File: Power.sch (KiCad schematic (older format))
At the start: 0 parts

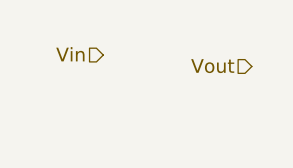
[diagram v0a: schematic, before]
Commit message: added SKY65366-21 schematic and footprint to library. Populated front end schematic with SKY and peripherial components. Added 3V6 output for power sub-schematic.
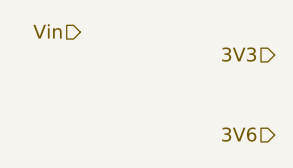
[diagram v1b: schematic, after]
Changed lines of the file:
@@
 Comment4 ""
 $EndDescr
-Text HLabel 3000 3300 0    60   Input ~ 0
+Text HLabel 2900 3200 0    60   Input ~ 0
 Vin
-Text HLabel 3650 3350 0    60   Input ~ 0
-Vout
+Text HLabel 3750 3300 0    60   Input ~ 0
+3V3
+Text HLabel 3750 3650 0    60   Input ~ 0
+3V6
 $EndSCHEMATC

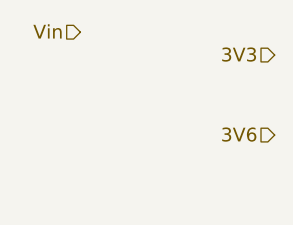
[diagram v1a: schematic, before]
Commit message: Fixed XOSC
-Changed 3V3 rail of XOSC to 1V8 as specified in datasheet
-Changed XOSC capacitor values to match the datasheet
-Added 1V8 rail to SFUSat-Radio.sch Transceiver and Power pages
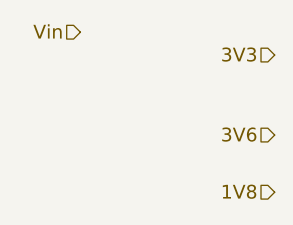
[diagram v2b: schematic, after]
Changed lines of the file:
@@
 Text HLabel 3750 3650 0    60   Input ~ 0
 3V6
+Text HLabel 3750 3900 0    60   Input ~ 0
+1V8
 $EndSCHEMATC

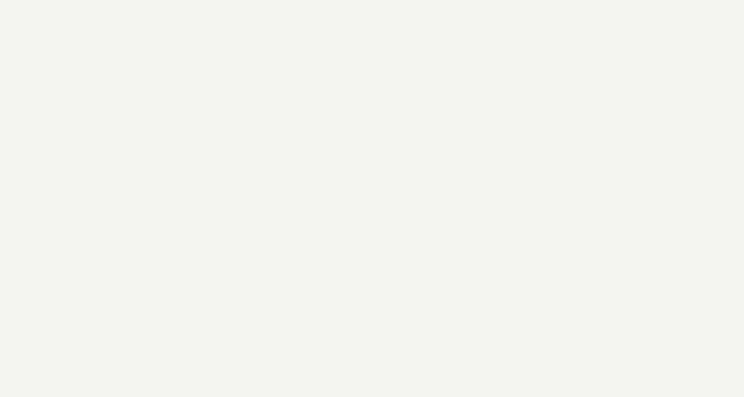
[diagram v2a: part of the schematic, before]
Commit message: Added schematic of RT9183HGM5 (TO263-5)
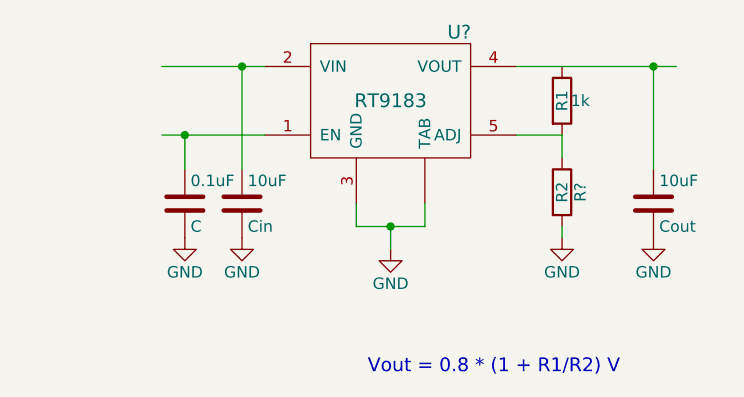
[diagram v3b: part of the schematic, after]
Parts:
- added 0.1uF: C, symbol C
- added 10uF: Cin, symbol C
- added 10uF: Cout, symbol C
- added 1k: R1, symbol R
- added R?: R2, symbol R
- added U?: RT9183, symbol RT9183
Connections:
- net labels added: GND
- wire segments 0 -> 13
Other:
- note added: "Vout = 0.8 * (1 + R1/R2) V\n"
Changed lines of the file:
@@
 Text HLabel 3750 3900 0    60   Input ~ 0
 1V8
+$Comp
+L RT9183 U?
+U 1 1 58770580
+P 5650 3000
+F 0 "U?" H 5950 3300 60  0000 C CNN
+F 1 "RT9183" H 5650 3000 60  0000 C CNN
+F 2 "" H 5650 3000 60  0001 C CNN
+F 3 "" H 5650 3000 60  0001 C CNN
+	1    5650 3000
+	1    0    0    -1
+$EndComp
+$Comp
+L C 10uF
+U 1 1 587706B0
+P 5000 3450
+F 0 "10uF" H 5025 3550 50  0000 L CNN
+F 1 "Cin" H 5025 3350 50  0000 L CNN
+F 2 "" H 5038 3300 50  0000 C CNN
+F 3 "" H 5000 3450 50  0000 C CNN
+	1    5000 3450
+	1    0    0    -1
+$EndComp
+$Comp
+L C 0.1uF
+U 1 1 58770789
+P 4750 3450
+F 0 "0.1uF" H 4775 3550 50  0000 L CNN
+F 1 "C" H 4775 3350 50  0000 L CNN
+F 2 "" H 4788 3300 50  0000 C CNN
+F 3 "" H 4750 3450 50  0000 C CNN
+	1    4750 3450
+	1    0    0    -1
+$EndComp
+$Comp
+L GND #PWR?
+U 1 1 58770941
+P 5650 3650
+F 0 "#PWR?" H 5650 3400 50  0001 C CNN
+F 1 "GND" H 5650 3500 50  0000 C CNN
+F 2 "" H 5650 3650 50  0000 C CNN
+F 3 "" H 5650 3650 50  0000 C CNN
+	1    5650 3650
+	1    0    0    -1
+$EndComp
+$Comp
+L C 10uF
+U 1 1 58770AC4
+P 6800 3450
+F 0 "10uF" H 6825 3550 50  0000 L CNN
+F 1 "Cout" H 6825 3350 50  0000 L CNN
+F 2 "" H 6838 3300 50  0000 C CNN
+F 3 "" H 6800 3450 50  0000 C CNN
+	1    6800 3450
+	1    0    0    -1
+$EndComp
+$Comp
+L GND #PWR?
+U 1 1 58770B93
+P 6800 3600
+F 0 "#PWR?" H 6800 3350 50  0001 C CNN
+F 1 "GND" H 6800 3450 50  0000 C CNN
+F 2 "" H 6800 3600 50  0000 C CNN
+F 3 "" H 6800 3600 50  0000 C CNN
+	1    6800 3600
+	1    0    0    -1
+$EndComp
+$Comp
+L GND #PWR?
+U 1 1 58770BD7
+P 6400 3600
+F 0 "#PWR?" H 6400 3350 50  0001 C CNN
+F 1 "GND" H 6400 3450 50  0000 C CNN
+F 2 "" H 6400 3600 50  0000 C CNN
+F 3 "" H 6400 3600 50  0000 C CNN
+	1    6400 3600
+	1    0    0    -1
+$EndComp
+$Comp
+L GND #PWR?
+U 1 1 58770CCB
+P 5000 3600
+F 0 "#PWR?" H 5000 3350 50  0001 C CNN
+F 1 "GND" H 5000 3450 50  0000 C CNN
+F 2 "" H 5000 3600 50  0000 C CNN
+F 3 "" H 5000 3600 50  0000 C CNN
+	1    5000 3600
+	1    0    0    -1
+$EndComp
+$Comp
+L GND #PWR?
+U 1 1 58770CE7
+P 4750 3600
+F 0 "#PWR?" H 4750 3350 50  0001 C CNN
+F 1 "GND" H 4750 3450 50  0000 C CNN
+F 2 "" H 4750 3600 50  0000 C CNN
+F 3 "" H 4750 3600 50  0000 C CNN
+	1    4750 3600
+	1    0    0    -1
+$EndComp
+Wire Wire Line
+	4650 2850 5100 2850
+Wire Wire Line
+	5000 2850 5000 3300
+Connection ~ 5000 2850
+Wire Wire Line
+	5100 3150 4650 3150
+Wire Wire Line
+	4750 3150 4750 3300
+Connection ~ 4750 3150
+Wire Wire Line
+	5500 3450 5500 3550
+Wire Wire Line
+	5800 3450 5800 3550
+Wire Wire Line
+	5800 3550 5500 3550
+Wire Wire Line
+	5650 3550 5650 3650
+Connection ~ 5650 3550
+Wire Wire Line
+	6200 2850 6900 2850
+Wire Wire Line
+	6800 2850 6800 3300
+Connection ~ 6800 2850
+Wire Wire Line
+	6200 3150 6400 3150
+Wire Wire Line
+	6400 3150 6400 3250
+Wire Wire Line
+	6400 3600 6400 3550
+$Comp
+L R R?
+U 1 1 58770EF4
+P 6400 3400
+F 0 "R?" V 6480 3400 50  0000 C CNN
+F 1 "R2" V 6400 3400 50  0000 C CNN
+F 2 "" V 6330 3400 50  0000 C CNN
+F 3 "" H 6400 3400 50  0000 C CNN
+	1    6400 3400
+	1    0    0    -1
+$EndComp
+$Comp
+L R 1k
+U 1 1 58770EC5
+P 6400 3000
+F 0 "1k" H 6480 3000 50  0000 C CNN
+F 1 "R1" V 6400 3000 50  0000 C CNN
+F 2 "" V 6330 3000 50  0000 C CNN
+F 3 "" H 6400 3000 50  0000 C CNN
+	1    6400 3000
+	1    0    0    -1
+$EndComp
+Text Notes 5550 4200 0    60   ~ 0
+Vout = 0.8 * (1 + R1/R2) V\n
 $EndSCHEMATC

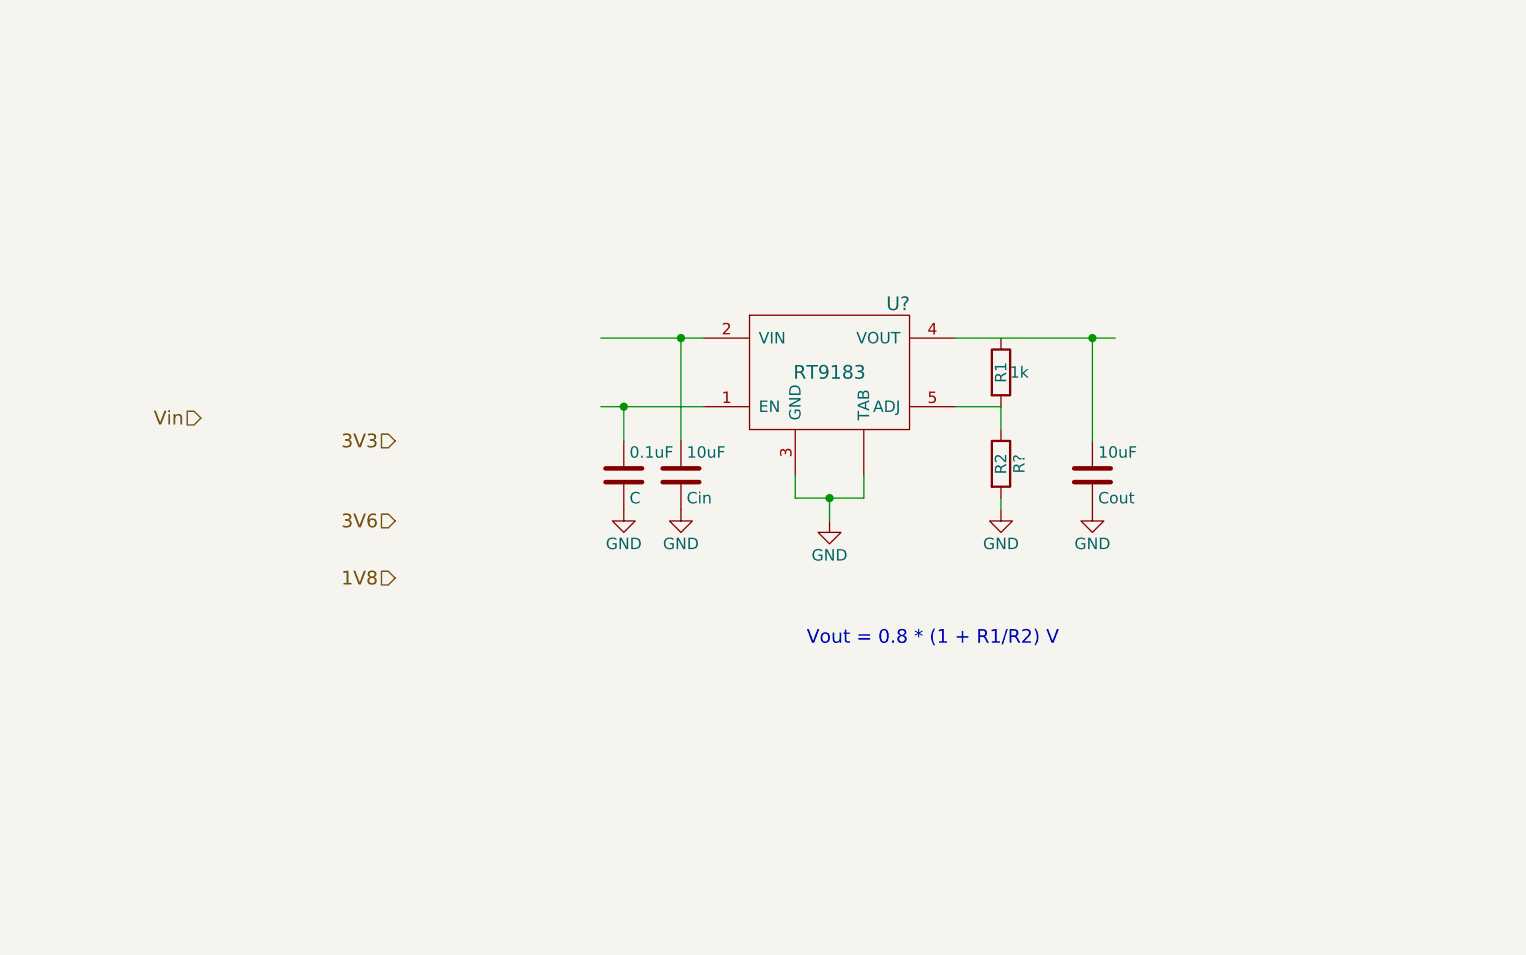
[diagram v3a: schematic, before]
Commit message: Added sch of TPS799 onto power sch
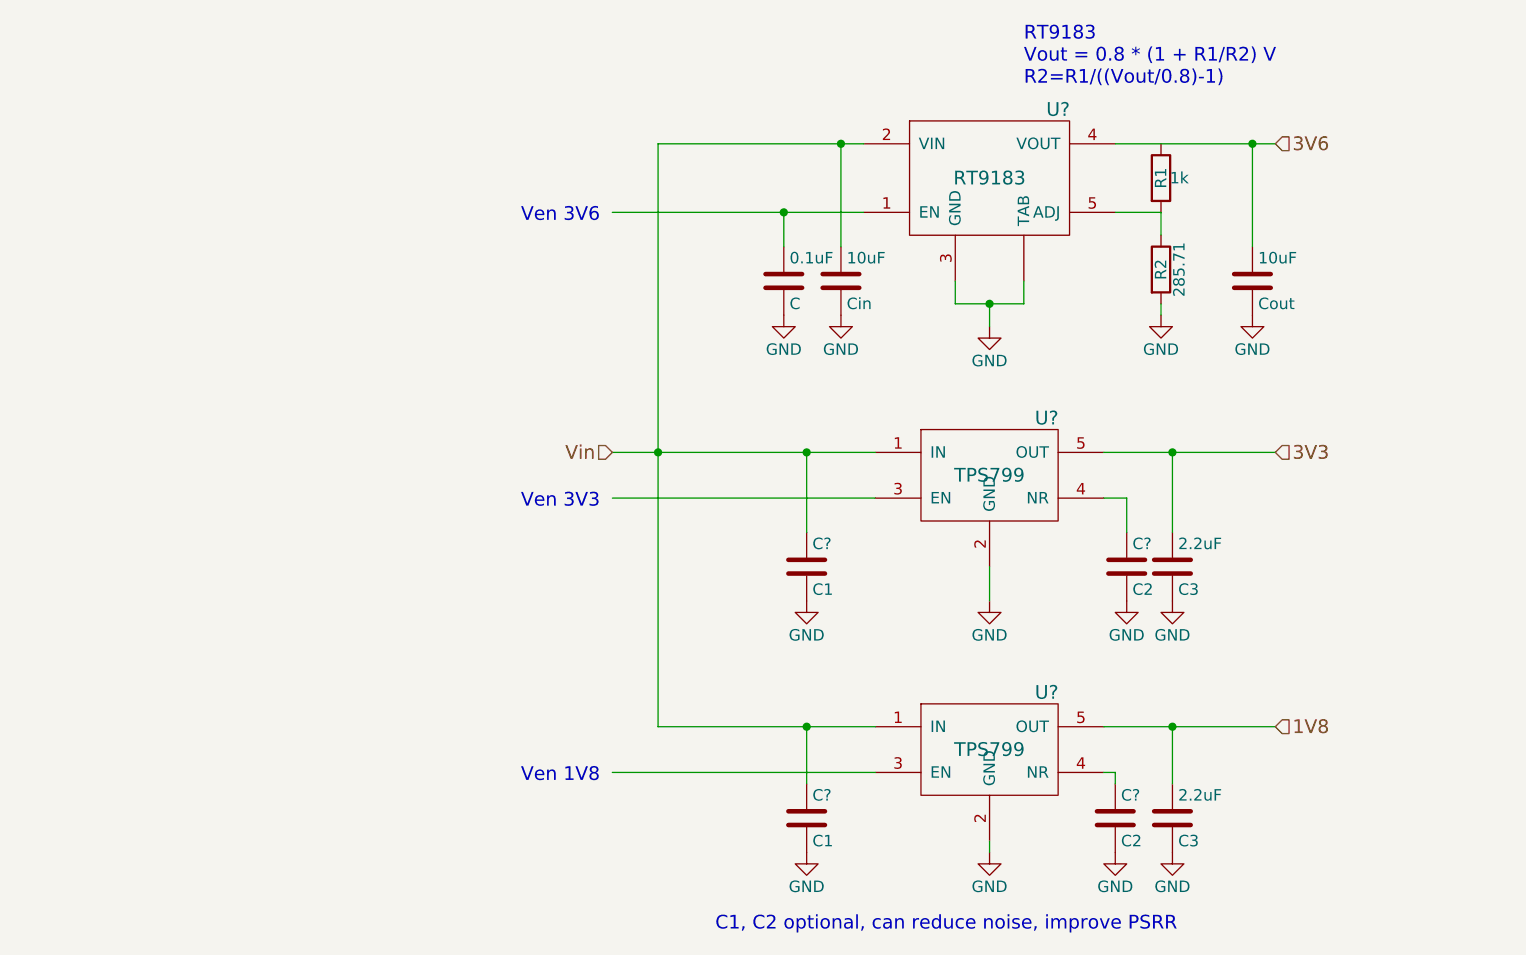
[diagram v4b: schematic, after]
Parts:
- added 2.2uF (x2): C3, symbol C
- added C? (x2): C2, symbol C
- added C? (x2): C1, symbol C
- added U? (x2): TPS799, symbol TPS799
- gave numbers to parts that had none: 1
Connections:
- wire segments 13 -> 30
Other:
- note added: "C1, C2 optional, can reduce noise, improve PSRR"
- note added: "RT9183\nVout = 0.8 * (1 + R1/R2) V\nR2=R1/((Vout/0.8)-1)"
- note added: "Ven 1V8"
- note added: "Ven 3V3"
- note added: "Ven 3V6"
- note removed: "Vout = 0.8 * (1 + R1/R2) V\n"
- moved on the sheet: 0.1uF, 10uF, 1k, 285.71, U?

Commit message: moved jumpers into respective schematics
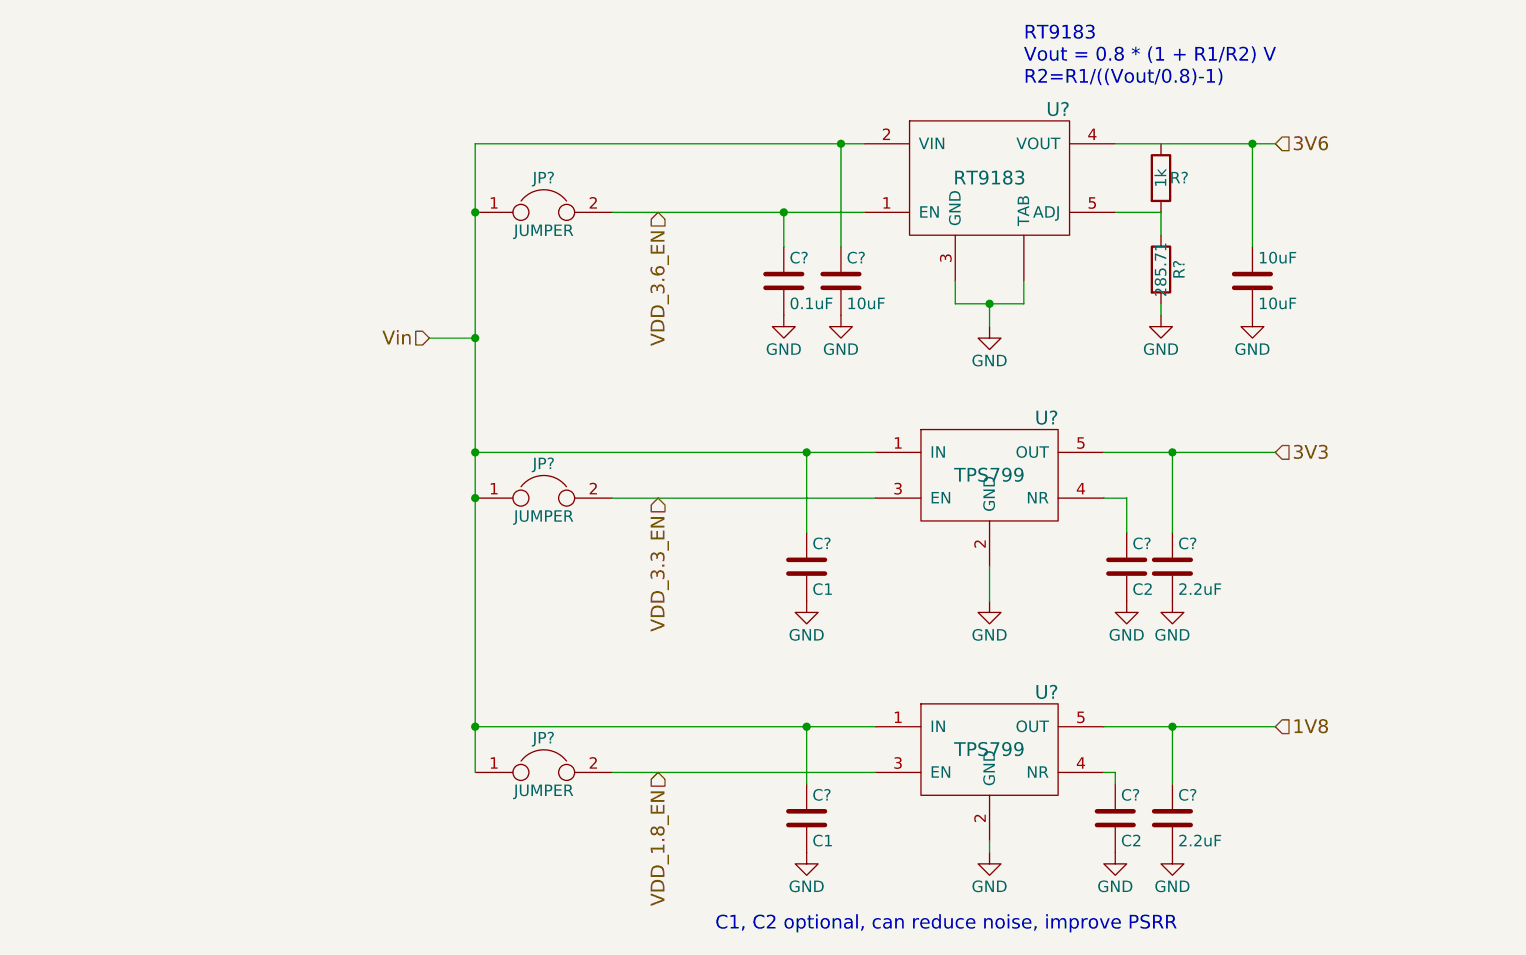
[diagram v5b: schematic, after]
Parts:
- added JP? (x3): JUMPER, symbol JUMPER
- 10uF: value Cout -> 10uF
- C?: renamed from 10uF; value Cin -> 10uF
- C?: renamed from 0.1uF; value C -> 0.1uF
- C? (x2): renamed from 2.2uF; value C3 -> 2.2uF
- R?: renamed from 1k; value R1 -> 1k
- R?: renamed from 285.71; value R2 -> 285.71
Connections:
- net labels added: VDD_1.8_EN, VDD_3.3_EN, VDD_3.6_EN
- wire segments 30 -> 31
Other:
- note removed: "Ven 1V8"
- note removed: "Ven 3V3"
- note removed: "Ven 3V6"
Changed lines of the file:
@@
 Comment4 ""
 $EndDescr
-Text HLabel 4700 3350 0    60   Input ~ 0
+Text HLabel 3900 2850 0    60   Input ~ 0
 Vin
 Text HLabel 7600 3350 2    60   Input ~ 0
@@
 $EndComp
 $Comp
-L C 10uF
+L C C?
 U 1 1 587706B0
 P 5700 2600
-F 0 "10uF" H 5725 2700 50  0000 L CNN
-F 1 "Cin" H 5725 2500 50  0000 L CNN
+F 0 "C?" H 5725 2700 50  0000 L CNN
+F 1 "10uF" H 5725 2500 50  0000 L CNN
 F 2 "" H 5738 2450 50  0000 C CNN
 F 3 "" H 5700 2600 50  0000 C CNN
@@
 $EndComp
 $Comp
-L C 0.1uF
+L C C?
 U 1 1 58770789
 P 5450 2600
-F 0 "0.1uF" H 5475 2700 50  0000 L CNN
-F 1 "C" H 5475 2500 50  0000 L CNN
+F 0 "C?" H 5475 2700 50  0000 L CNN
+F 1 "0.1uF" H 5475 2500 50  0000 L CNN
 F 2 "" H 5488 2450 50  0000 C CNN
 F 3 "" H 5450 2600 50  0000 C CNN
@@
 P 7500 2600
 F 0 "10uF" H 7525 2700 50  0000 L CNN
-F 1 "Cout" H 7525 2500 50  0000 L CNN
+F 1 "10uF" H 7525 2500 50  0000 L CNN
 F 2 "" H 7538 2450 50  0000 C CNN
 F 3 "" H 7500 2600 50  0000 C CNN
@@
 	1    0    0    -1
 $EndComp
-Wire Wire Line
-	4900 2000 5800 2000
-Wire Wire Line
-	5700 2000 5700 2450
-Connection ~ 5700 2000
-Wire Wire Line
-	4700 2300 5800 2300
-Wire Wire Line
-	5450 2300 5450 2450
-Connection ~ 5450 2300
-Wire Wire Line
-	6200 2600 6200 2700
-Wire Wire Line
-	6500 2600 6500 2700
-Wire Wire Line
-	6500 2700 6200 2700
-Wire Wire Line
-	6350 2700 6350 2800
-Connection ~ 6350 2700
-Wire Wire Line
-	6900 2000 7600 2000
-Wire Wire Line
-	7500 2000 7500 2450
-Connection ~ 7500 2000
-Wire Wire Line
-	6900 2300 7100 2300
-Wire Wire Line
-	7100 2300 7100 2400
-Wire Wire Line
-	7100 2750 7100 2700
-$Comp
-L R 285.71
+$Comp
+L R R?
 U 1 1 58770EF4
 P 7100 2550
-F 0 "285.71" V 7180 2550 50  0000 C CNN
-F 1 "R2" V 7100 2550 50  0000 C CNN
+F 0 "R?" V 7180 2550 50  0000 C CNN
+F 1 "285.71" V 7100 2550 50  0000 C CNN
 F 2 "" V 7030 2550 50  0000 C CNN
 F 3 "" H 7100 2550 50  0000 C CNN
@@
 $EndComp
 $Comp
-L R 1k
+L R R?
 U 1 1 58770EC5
 P 7100 2150
-F 0 "1k" H 7180 2150 50  0000 C CNN
-F 1 "R1" V 7100 2150 50  0000 C CNN
+F 0 "R?" H 7180 2150 50  0000 C CNN
+F 1 "1k" V 7100 2150 50  0000 C CNN
 F 2 "" V 7030 2150 50  0000 C CNN
 F 3 "" H 7100 2150 50  0000 C CNN
@@
 	1    0    0    -1
 $EndComp
-Wire Wire Line
-	4700 3350 5850 3350
-Wire Wire Line
-	4700 3550 5850 3550
-Wire Wire Line
-	6350 3850 6350 4000
-Wire Wire Line
-	6850 3550 6950 3550
-Wire Wire Line
-	6950 3550 6950 3700
-Wire Wire Line
-	6850 3350 7600 3350
-Wire Wire Line
-	7150 3350 7150 3700
-Connection ~ 7150 3350
 $Comp
 L GND #PWR?
@@
 $EndComp
 $Comp
-L C 2.2uF
+L C C?
 U 1 1 5879DAAB
 P 7150 3850
-F 0 "2.2uF" H 7175 3950 50  0000 L CNN
-F 1 "C3" H 7175 3750 50  0000 L CNN
+F 0 "C?" H 7175 3950 50  0000 L CNN
+F 1 "2.2uF" H 7175 3750 50  0000 L CNN
 F 2 "" H 7188 3700 50  0000 C CNN
 F 3 "" H 7150 3850 50  0000 C CNN
@@
 	1    0    0    -1
 $EndComp
-Wire Wire Line
-	5550 3350 5550 3700
-Connection ~ 5550 3350
 $Comp
 L GND #PWR?
@@
 	1    0    0    -1
 $EndComp
-Wire Wire Line
-	4900 4550 5850 4550
-Connection ~ 5550 4550
 $Comp
 L C C?
@@
 $EndComp
 $Comp
-L C 2.2uF
+L C C?
 U 1 1 587A204E
 P 7150 4950
-F 0 "2.2uF" H 7175 5050 50  0000 L CNN
-F 1 "C3" H 7175 4850 50  0000 L CNN
+F 0 "C?" H 7175 5050 50  0000 L CNN
+F 1 "2.2uF" H 7175 4850 50  0000 L CNN
 F 2 "" H 7188 4800 50  0000 C CNN
 F 3 "" H 7150 4950 50  0000 C CNN
@@
 	1    0    0    -1
 $EndComp
-Wire Wire Line
-	6850 4750 6900 4750
-Wire Wire Line
-	6900 4750 6900 4800
-Wire Wire Line
-	6850 4550 7600 4550
-Wire Wire Line
-	7150 4550 7150 4800
-Connection ~ 7150 4550
-Wire Wire Line
-	4700 4750 5850 4750
 $Comp
 L GND #PWR?
@@
 	1    0    0    -1
 $EndComp
-Wire Wire Line
-	6350 5050 6350 5100
-Wire Wire Line
-	5550 4800 5550 4550
-Wire Wire Line
-	4900 2000 4900 4550
-Connection ~ 4900 3350
 Text Notes 5150 5450 0    60   ~ 0
 C1, C2 optional, can reduce noise, improve PSRR
-Text Notes 4300 2350 0    60   ~ 0
-Ven 3V6
-Text Notes 4300 3600 0    60   ~ 0
-Ven 3V3
-Text Notes 4300 4800 0    60   ~ 0
-Ven 1V8
+Text HLabel 4900 4750 3    60   Input ~ 0
+VDD_1.8_EN
+Text HLabel 4900 3550 3    60   Input ~ 0
+VDD_3.3_EN
+Text HLabel 4900 2300 3    60   Input ~ 0
+VDD_3.6_EN
+$Comp
+L JUMPER JP?
+U 1 1 587BADC1
+P 4400 2300
+F 0 "JP?" H 4400 2450 50  0000 C CNN
+F 1 "JUMPER" H 4400 2220 50  0000 C CNN
+F 2 "" H 4400 2300 50  0000 C CNN
+F 3 "" H 4400 2300 50  0000 C CNN
+	1    4400 2300
+	1    0    0    -1
+$EndComp
+$Comp
+L JUMPER JP?
+U 1 1 587BAE6A
+P 4400 3550
+F 0 "JP?" H 4400 3700 50  0000 C CNN
+F 1 "JUMPER" H 4400 3470 50  0000 C CNN
+F 2 "" H 4400 3550 50  0000 C CNN
+F 3 "" H 4400 3550 50  0000 C CNN
+	1    4400 3550
+	1    0    0    -1
+$EndComp
+$Comp
+L JUMPER JP?
+U 1 1 587BAFA3
+P 4400 4750
+F 0 "JP?" H 4400 4900 50  0000 C CNN
+F 1 "JUMPER" H 4400 4670 50  0000 C CNN
+F 2 "" H 4400 4750 50  0000 C CNN
+F 3 "" H 4400 4750 50  0000 C CNN
+	1    4400 4750
+	1    0    0    -1
+$EndComp
+Wire Wire Line
+	4100 2000 5800 2000
+Wire Wire Line
+	5700 2000 5700 2450
+Connection ~ 5700 2000
+Wire Wire Line
+	4700 2300 5800 2300
+Wire Wire Line
+	5450 2300 5450 2450
+Connection ~ 5450 2300
+Wire Wire Line
+	6200 2600 6200 2700
+Wire Wire Line
+	6500 2600 6500 2700
+Wire Wire Line
+	6500 2700 6200 2700
+Wire Wire Line
+	6350 2700 6350 2800
+Connection ~ 6350 2700
+Wire Wire Line
+	6900 2000 7600 2000
+Wire Wire Line
+	7500 2000 7500 2450
+Connection ~ 7500 2000
+Wire Wire Line
+	6900 2300 7100 2300
+Wire Wire Line
+	7100 2300 7100 2400
+Wire Wire Line
+	7100 2750 7100 2700
+Wire Wire Line
+	4700 3550 5850 3550
+Wire Wire Line
+	6350 3850 6350 4000
+Wire Wire Line
+	6850 3550 6950 3550
+Wire Wire Line
+	6950 3550 6950 3700
+Wire Wire Line
+	6850 3350 7600 3350
+Wire Wire Line
+	7150 3350 7150 3700
+Connection ~ 7150 3350
+Wire Wire Line
+	5550 3350 5550 3700
+Connection ~ 5550 3350
+Wire Wire Line
+	4100 4550 5850 4550
+Connection ~ 5550 4550
+Wire Wire Line
+	6850 4750 6900 4750
+Wire Wire Line
+	6900 4750 6900 4800
+Wire Wire Line
+	6850 4550 7600 4550
+Wire Wire Line
+	7150 4550 7150 4800
+Connection ~ 7150 4550
+Wire Wire Line
+	4700 4750 5850 4750
+Wire Wire Line
+	6350 5050 6350 5100
+Wire Wire Line
+	5550 4800 5550 4550
+Wire Wire Line
+	4100 2000 4100 4750
+Connection ~ 4100 3550
+Wire Wire Line
+	4100 3350 5850 3350
+Connection ~ 4100 3350
+Connection ~ 4100 4550
+Connection ~ 4100 2300
+Wire Wire Line
+	4100 2850 3900 2850
+Connection ~ 4100 2850
 $EndSCHEMATC
